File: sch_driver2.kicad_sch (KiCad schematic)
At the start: 19 parts, among them Q2 PSMN4R0-30YLDX, U1 ADA4099-2xR, U12 TS5A3159ADCK, U22 OPA365AIDBV, U4 ADA4099-1

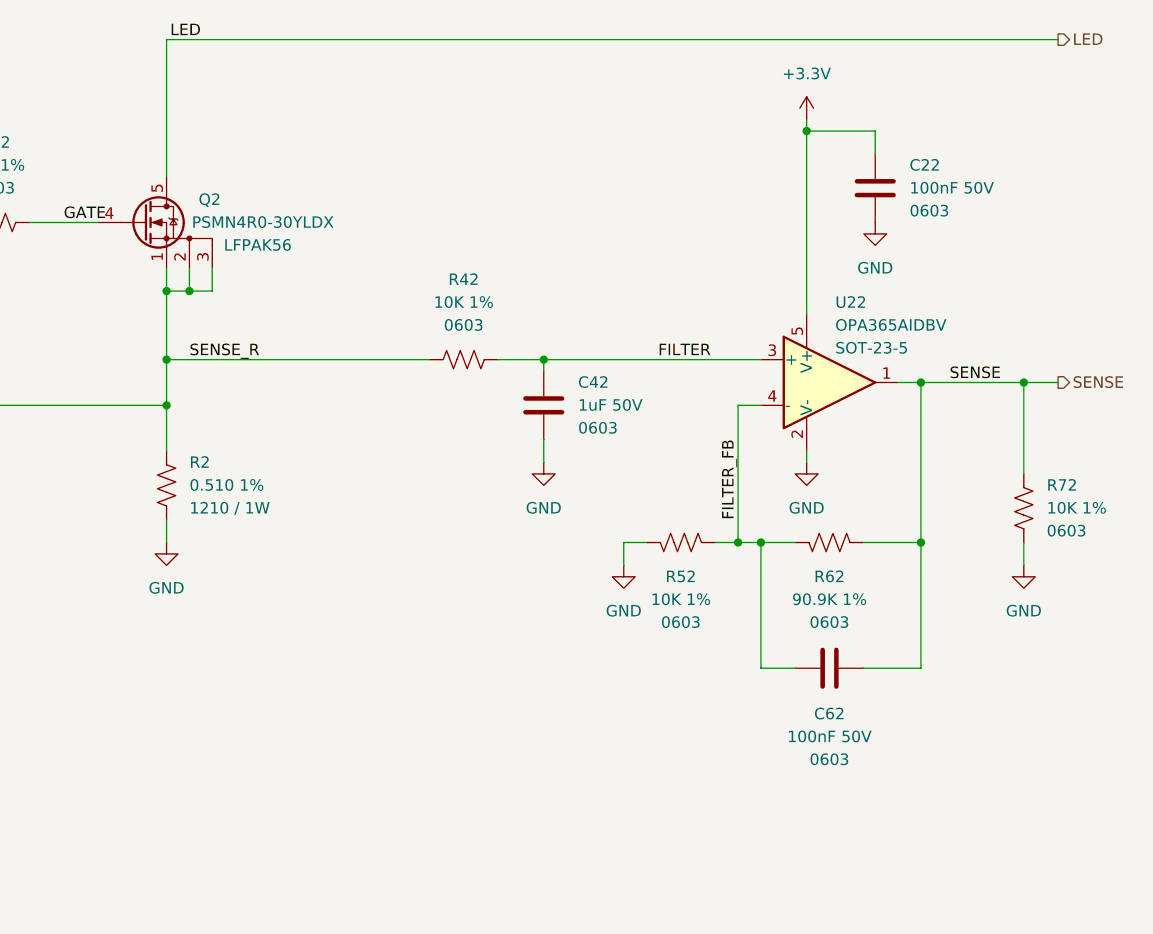
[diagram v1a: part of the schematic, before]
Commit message: Initial placement on 45 x 30 mm outline. Dropped sense apms. Switch to two 2x6 connectors.
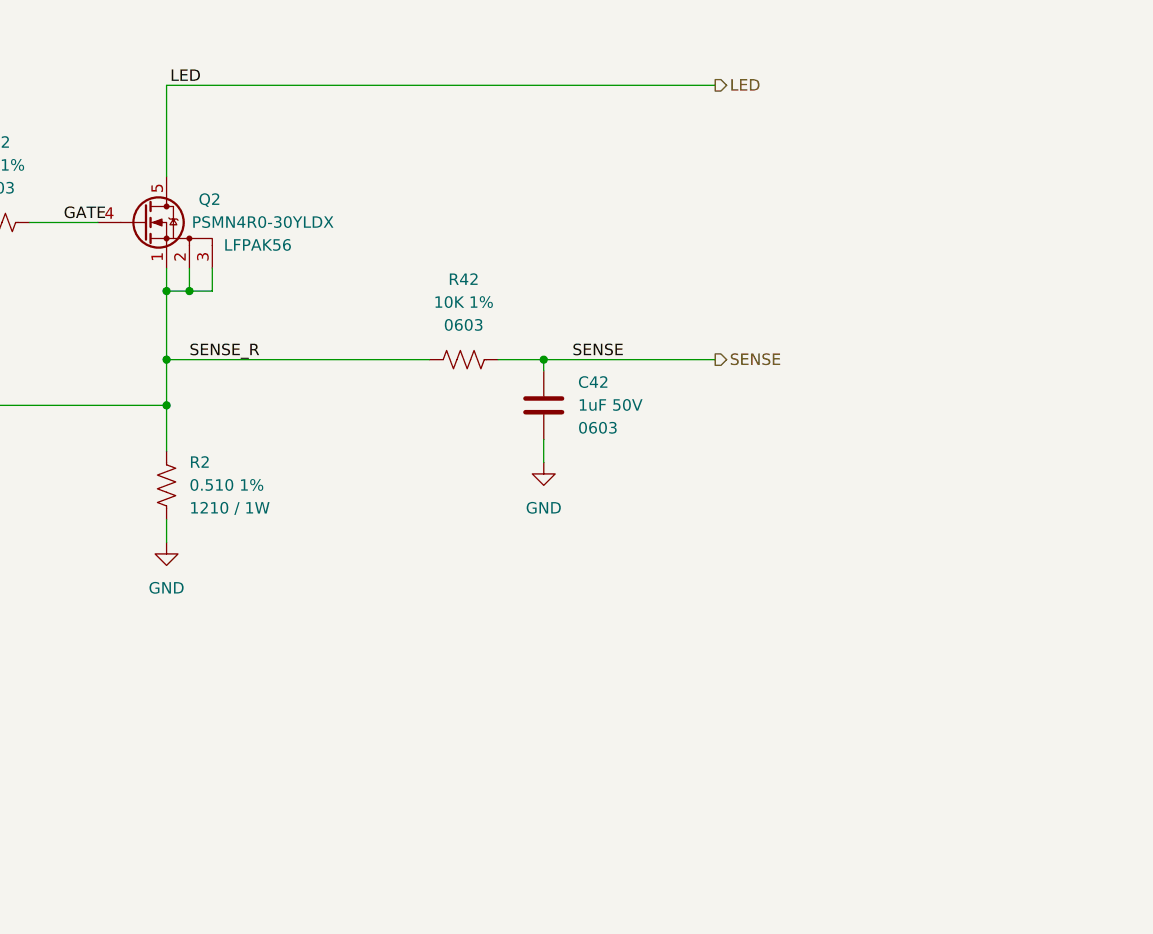
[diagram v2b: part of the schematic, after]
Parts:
- removed C22, C62: 100nF 50V, $Local:C_0603_1608Metric, symbol $Local:C_0603_100NF_50V
- removed R52, R72: 10K 1%, $Local:R_0603_1608Metric, symbol $Local:R_0603_10K
- removed R62: 90.9K 1%, $Local:R_0603_1608Metric, symbol $Local:R_0603_10K
- removed U22: OPA365AIDBV, $Local:SOT-23-5, symbol $Local:OPA365AIDBV
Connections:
- net FILTER is gone; now on net SENSE: C42.1, R42.1
